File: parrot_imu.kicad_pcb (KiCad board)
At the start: 2 copper layers, 50 x 100 mm, 29 parts, among them J1 Conn_01x02_Male, J2 SI-60062-F, J3 TB005-762-02BE, U1 TR05S3V3, U2 VR10S05, U3 Spark_fun_ICM-20948, U4 Teensy4.1, U5 TJA1441AT/0Z, U6 ESDCAN24-2BLY

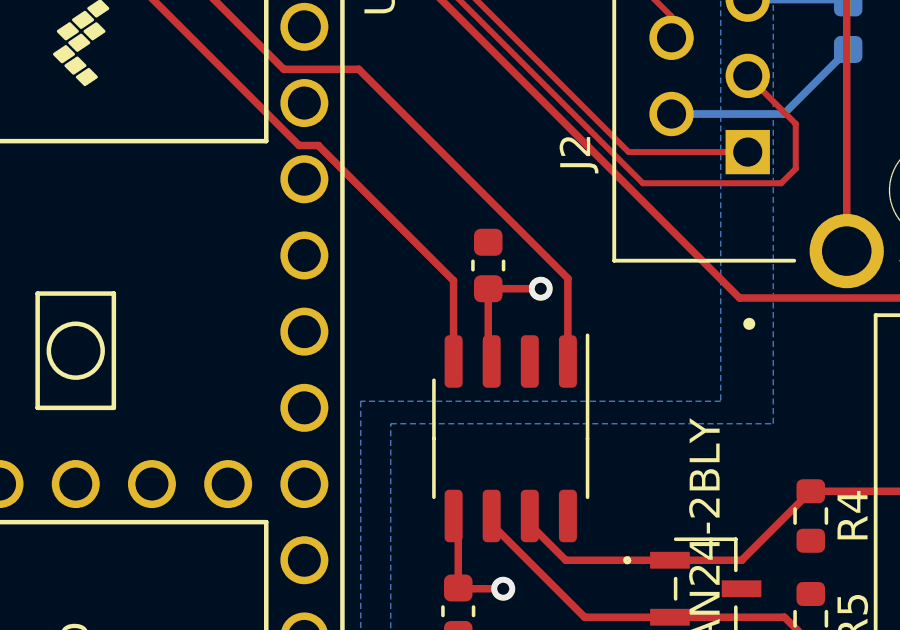
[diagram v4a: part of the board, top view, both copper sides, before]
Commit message: fix unconnected plane error
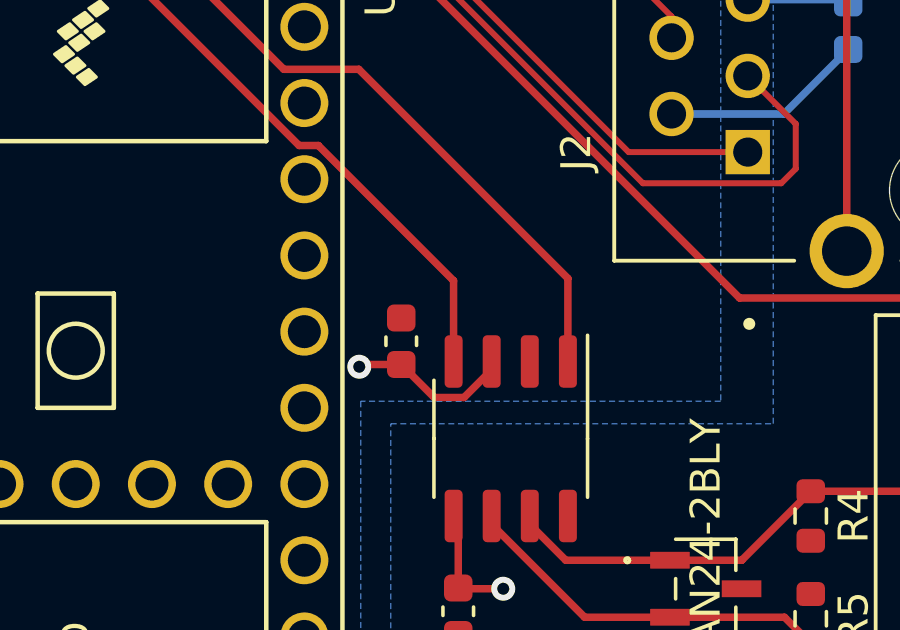
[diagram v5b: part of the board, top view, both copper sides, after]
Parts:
- moved C5 3.85 mm to (70.8, 101.2)
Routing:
- net +5V: track 12.0 -> 13.4 mm
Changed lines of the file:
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@@
   )
   (footprint "Capacitor_SMD:C_0603_1608Metric" (layer "F.Cu")
-    (at 73.75 98.725 90)
+    (at 70.85 101.25 90)
     (descr "Capacitor SMD 0603 (1608 Metric), square (rectangular) end terminal, IPC_7351 nominal, (Body size source: IPC-SM-782 page 76, https://www.pcb-3d.com/wordpress/wp-content/uploads/ipc-sm-782a_amendment_1_and_2.pdf), generated with kicad-footprint-generator")
     (tags "capacitor")
@@
   (segment (start 79.86 86.055) (end 87.191571 86.055) (width 0.25) (layer "B.Cu") (net 2))
   (segment (start 85.64 89.865) (end 85.75 89.975) (width 0.25) (layer "B.Cu") (net 2))
-  (segment (start 73.75 101.81) (end 73.865 101.925) (width 0.25) (layer "F.Cu") (net 3))
   (segment (start 59.5 121.75) (end 61.425 121.75) (width 0.25) (layer "F.Cu") (net 3))
+  (segment (start 70.85 102.025) (end 71.95 103.125) (width 0.25) (layer "F.Cu") (net 3))
   (segment (start 59.776393 130.46) (end 56.316393 127) (width 0.25) (layer "F.Cu") (net 3))
-  (segment (start 75.5 99.5) (end 73.75 99.5) (width 0.25) (layer "F.Cu") (net 3))
+  (segment (start 72.941751 103.125) (end 73.865 102.201751) (width 0.25) (layer "F.Cu") (net 3))
   (segment (start 56.316393 127) (end 55.43238 127) (width 0.25) (layer "F.Cu") (net 3))
-  (segment (start 73.75 99.5) (end 73.75 101.81) (width 0.25) (layer "F.Cu") (net 3))
+  (segment (start 70.85 102.025) (end 69.525 102.025) (width 0.25) (layer "F.Cu") (net 3))
+  (segment (start 69.525 102.025) (end 69.45 102.1) (width 0.25) (layer "F.Cu") (net 3))
   (segment (start 61.425 121.75) (end 61.5 121.675) (width 0.25) (layer "F.Cu") (net 3))
+  (segment (start 73.865 102.201751) (end 73.865 101.925) (width 0.25) (layer "F.Cu") (net 3))
+  (segment (start 71.95 103.125) (end 72.941751 103.125) (width 0.25) (layer "F.Cu") (net 3))
   (via (at 59.5 121.75) (size 0.8) (drill 0.4) (layers "F.Cu" "B.Cu") (free) (net 3))
-  (via (at 75.5 99.5) (size 0.8) (drill 0.4) (layers "F.Cu" "B.Cu") (free) (net 3))
+  (via (at 69.45 102.1) (size 0.8) (drill 0.4) (layers "F.Cu" "B.Cu") (free) (net 3))
   (segment (start 91.915 117.835) (end 92 117.75) (width 0.25) (layer "F.Cu") (net 4))
   (segment (start 72.775 109.5) (end 72.75 109.475) (width 0.25) (layer "F.Cu") (net 4))

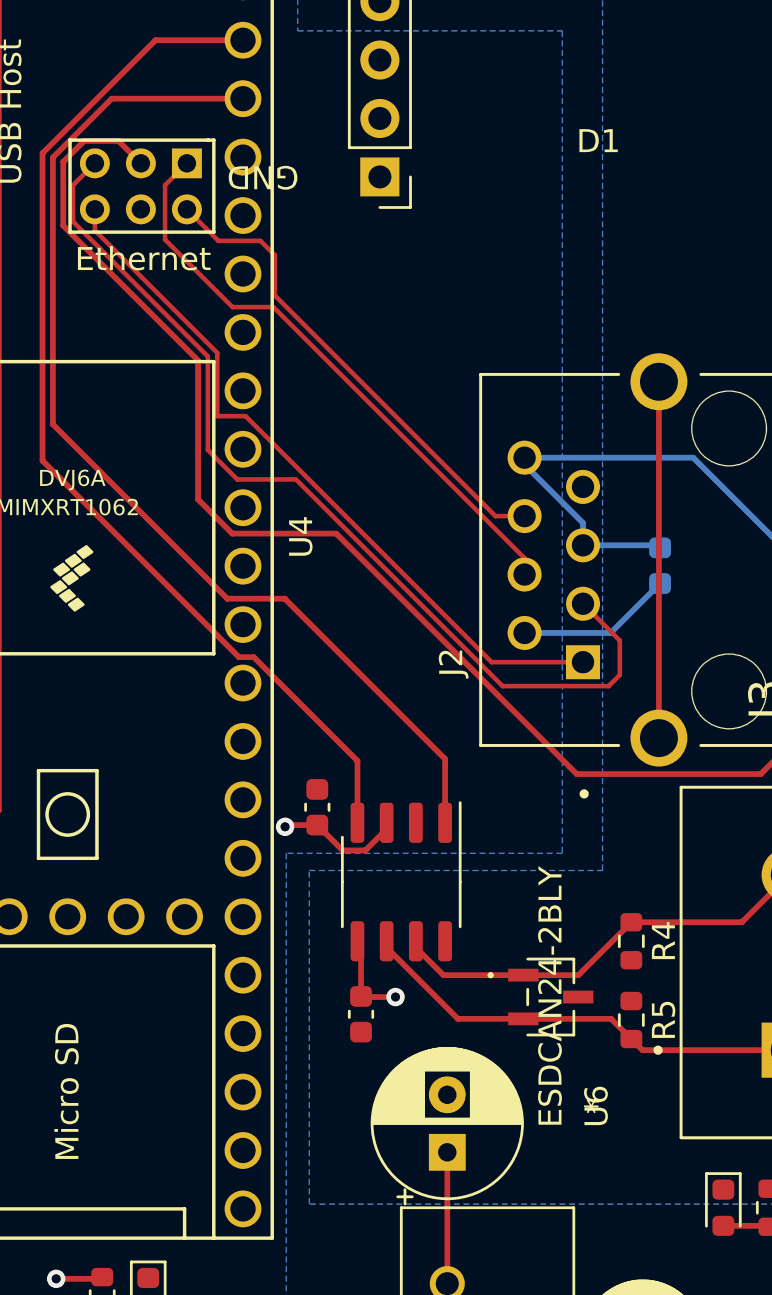
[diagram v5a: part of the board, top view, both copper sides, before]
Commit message: fix errors with unconnected components
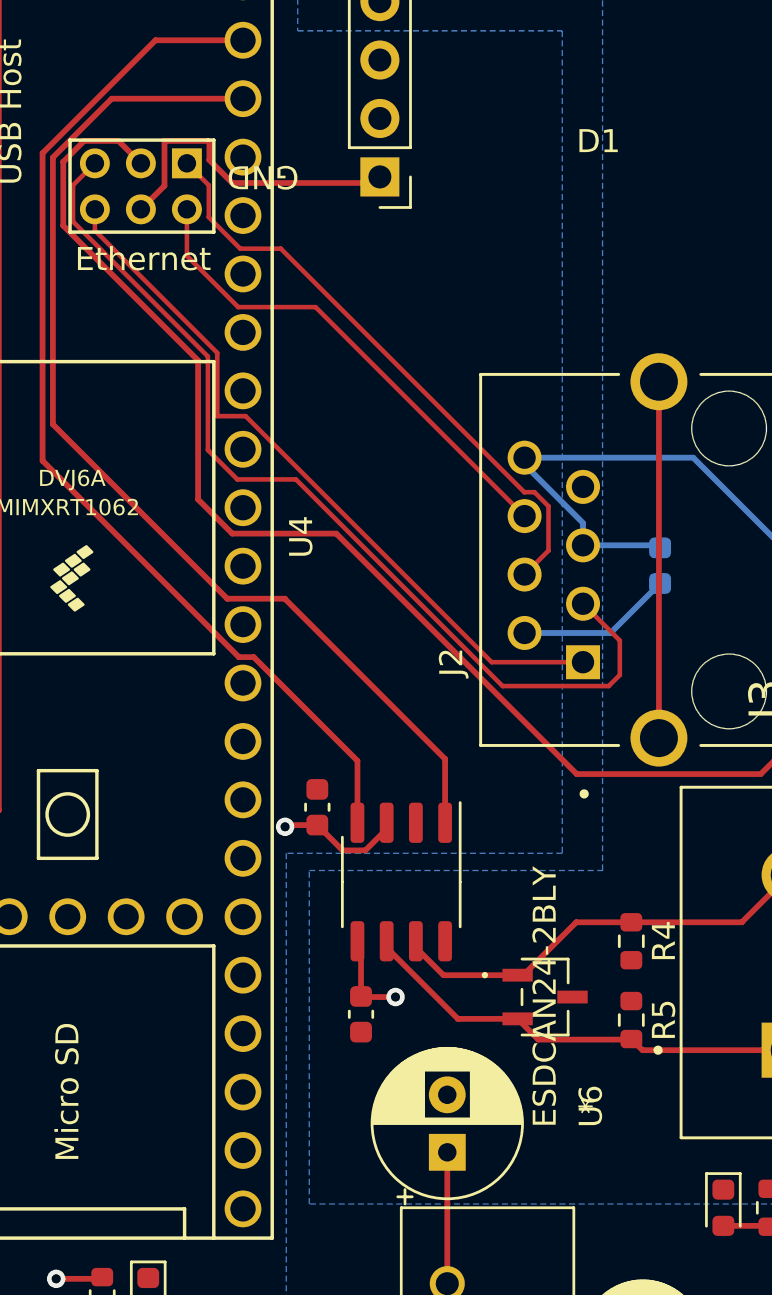
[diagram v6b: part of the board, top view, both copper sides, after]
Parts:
- moved U6 0.25 mm to (80.8, 109.5)
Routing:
- net GND: track 31.7 -> 45.8 mm
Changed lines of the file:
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@@
   )
   (footprint "parrot_imu:ESDCAN24-2BLY" (layer "F.Cu")
-    (at 81 109.5 -90)
+    (at 80.75 109.5 -90)
     (property "Sheetfile" "parrot_imu.kicad_sch")
     (property "Sheetname" "")
@@
   (segment (start 84 130) (end 76.5 130) (width 0.25) (layer "F.Cu") (net 1))
   (segment (start 59.816393 135.5) (end 59.776393 135.54) (width 0.25) (layer "F.Cu") (net 1))
+  (segment (start 64.2066 72.285) (end 64.2066 74.235) (width 0.25) (layer "F.Cu") (net 2))
+  (segment (start 66.1566 73.117591) (end 66.1566 72.285) (width 0.25) (layer "F.Cu") (net 2))
   (segment (start 93 125.625) (end 93 124.4125) (width 0.25) (layer "F.Cu") (net 2))
+  (segment (start 66.1566 72.285) (end 64.2066 72.285) (width 0.25) (layer "F.Cu") (net 2))
+  (segment (start 64.2066 74.235) (end 63.1816 75.26) (width 0.25) (layer "F.Cu") (net 2))
+  (segment (start 73.57 73.85) (end 73.305 74.115) (width 0.25) (layer "F.Cu") (net 2))
+  (segment (start 73.305 74.115) (end 67.154009 74.115) (width 0.25) (layer "F.Cu") (net 2))
   (segment (start 88 130) (end 92 130) (width 0.25) (layer "F.Cu") (net 2))
+  (segment (start 67.154009 74.115) (end 66.1566 73.117591) (width 0.25) (layer "F.Cu") (net 2))
   (via (at 92 130) (size 0.8) (drill 0.4) (layers "F.Cu" "B.Cu") (free) (net 2))
   (via (at 93 124.4125) (size 0.8) (drill 0.4) (layers "F.Cu" "B.Cu") (free) (net 2))
@@
   (segment (start 60.2316 74.21) (end 60.2316 75.794924) (width 0.2) (layer "F.Cu") (net 10))
   (segment (start 60.2316 75.794924) (end 66.093338 81.656662) (width 0.2) (layer "F.Cu") (net 10))
-  (segment (start 64.2316 74.21) (end 64.2316 76.577235) (width 0.2) (layer "F.Cu") (net 11))
-  (segment (start 65.1816 73.26) (end 64.2316 74.21) (width 0.2) (layer "F.Cu") (net 11))
-  (segment (start 79.86 90.425686) (end 79.86 91.135) (width 0.2) (layer "F.Cu") (net 11))
-  (segment (start 67.164365 79.51) (end 68.944314 79.51) (width 0.2) (layer "F.Cu") (net 11))
-  (segment (start 64.2316 76.577235) (end 67.164365 79.51) (width 0.2) (layer "F.Cu") (net 11))
-  (segment (start 68.944314 79.51) (end 79.86 90.425686) (width 0.2) (layer "F.Cu") (net 11))
-  (segment (start 78.595 88.595) (end 69 79) (width 0.2) (layer "F.Cu") (net 12))
-  (segment (start 79.86 88.595) (end 78.595 88.595) (width 0.2) (layer "F.Cu") (net 12))
-  (segment (start 69 77.25) (end 68.38 76.63) (width 0.2) (layer "F.Cu") (net 12))
-  (segment (start 69 79) (end 69 77.25) (width 0.2) (layer "F.Cu") (net 12))
-  (segment (start 66.5516 76.63) (end 65.1816 75.26) (width 0.2) (layer "F.Cu") (net 12))
-  (segment (start 68.38 76.63) (end 66.5516 76.63) (width 0.2) (layer "F.Cu") (net 12))
+  (segment (start 80.899 88.164632) (end 80.899 90.096) (width 0.2) (layer "F.Cu") (net 11))
+  (segment (start 80.290368 87.556) (end 80.899 88.164632) (width 0.2) (layer "F.Cu") (net 11))
+  (segment (start 79.85 87.556) (end 80.290368 87.556) (width 0.2) (layer "F.Cu") (net 11))
+  (segment (start 66.1316 74.21) (end 66.1316 75.6016) (width 0.2) (layer "F.Cu") (net 11))
+  (segment (start 69.264 76.97) (end 79.85 87.556) (width 0.2) (layer "F.Cu") (net 11))
+  (segment (start 66.1316 75.6016) (end 67.5 76.97) (width 0.2) (layer "F.Cu") (net 11))
+  (segment (start 67.5 76.97) (end 69.264 76.97) (width 0.2) (layer "F.Cu") (net 11))
+  (segment (start 65.1816 73.26) (end 66.1316 74.21) (width 0.2) (layer "F.Cu") (net 11))
+  (segment (start 80.899 90.096) (end 79.86 91.135) (width 0.2) (layer "F.Cu") (net 11))
+  (segment (start 65.1816 75.26) (end 65.1816 77.2816) (width 0.2) (layer "F.Cu") (net 12))
+  (segment (start 70.775 79.51) (end 79.86 88.595) (width 0.2) (layer "F.Cu") (net 12))
+  (segment (start 67.41 79.51) (end 70.775 79.51) (width 0.2) (layer "F.Cu") (net 12))
+  (segment (start 65.1816 77.2816) (end 67.41 79.51) (width 0.2) (layer "F.Cu") (net 12))
+  (segment (start 84.5 111.325) (end 84.985 111.81) (width 0.25) (layer "F.Cu") (net 13))
+  (segment (start 84.475 111.35) (end 84.5 111.325) (width 0.25) (layer "F.Cu") (net 13))
+  (segment (start 73.865 107.075) (end 73.865 107.351751) (width 0.25) (layer "F.Cu") (net 13))
+  (segment (start 80.45624 111.35) (end 84.475 111.35) (width 0.25) (layer "F.Cu") (net 13))
+  (segment (start 79.5562 110.44996) (end 80.45624 111.35) (width 0.25) (layer "F.Cu") (net 13))
   (segment (start 73.865 107.351751) (end 76.963209 110.44996) (width 0.25) (layer "F.Cu") (net 13))
-  (segment (start 83.62496 110.44996) (end 84.5 111.325) (width 0.25) (layer "F.Cu") (net 13))
-  (segment (start 73.865 107.075) (end 73.865 107.351751) (width 0.25) (layer "F.Cu") (net 13))
-  (segment (start 84.5 111.325) (end 84.985 111.81) (width 0.25) (layer "F.Cu") (net 13))
-  (segment (start 76.963209 110.44996) (end 79.8062 110.44996) (width 0.25) (layer "F.Cu") (net 13))
-  (segment (start 79.8062 110.44996) (end 83.62496 110.44996) (width 0.25) (layer "F.Cu") (net 13))
+  (segment (start 76.963209 110.44996) (end 79.5562 110.44996) (width 0.25) (layer "F.Cu") (net 13))
   (segment (start 84.985 111.81) (end 91.3625 111.81) (width 0.25) (layer "F.Cu") (net 13))
+  (segment (start 89.3025 106.25) (end 91.3625 104.19) (width 0.25) (layer "F.Cu") (net 14))
+  (segment (start 82.10624 106.25) (end 84.5 106.25) (width 0.25) (layer "F.Cu") (net 14))
   (segment (start 75.135 107.075) (end 75.135 107.351751) (width 0.25) (layer "F.Cu") (net 14))
-  (segment (start 82.19996 108.55004) (end 84.5 106.25) (width 0.25) (layer "F.Cu") (net 14))
-  (segment (start 76.333289 108.55004) (end 79.8062 108.55004) (width 0.25) (layer "F.Cu") (net 14))
-  (segment (start 89.3025 106.25) (end 91.3625 104.19) (width 0.25) (layer "F.Cu") (net 14))
   (segment (start 75.135 107.351751) (end 76.333289 108.55004) (width 0.25) (layer "F.Cu") (net 14))
   (segment (start 84.5 106.25) (end 89.3025 106.25) (width 0.25) (layer "F.Cu") (net 14))
-  (segment (start 79.8062 108.55004) (end 82.19996 108.55004) (width 0.25) (layer "F.Cu") (net 14))
+  (segment (start 79.8062 108.55004) (end 82.10624 106.25) (width 0.25) (layer "F.Cu") (net 14))
+  (segment (start 76.333289 108.55004) (end 79.8062 108.55004) (width 0.25) (layer "F.Cu") (net 14))
   (segment (start 99.25 52.75) (end 99.25 61.5) (width 0.25) (layer "F.Cu") (net 19))
   (segment (start 52.38 62.83) (end 64.71 50.5) (width 0.25) (layer "F.Cu") (net 19))

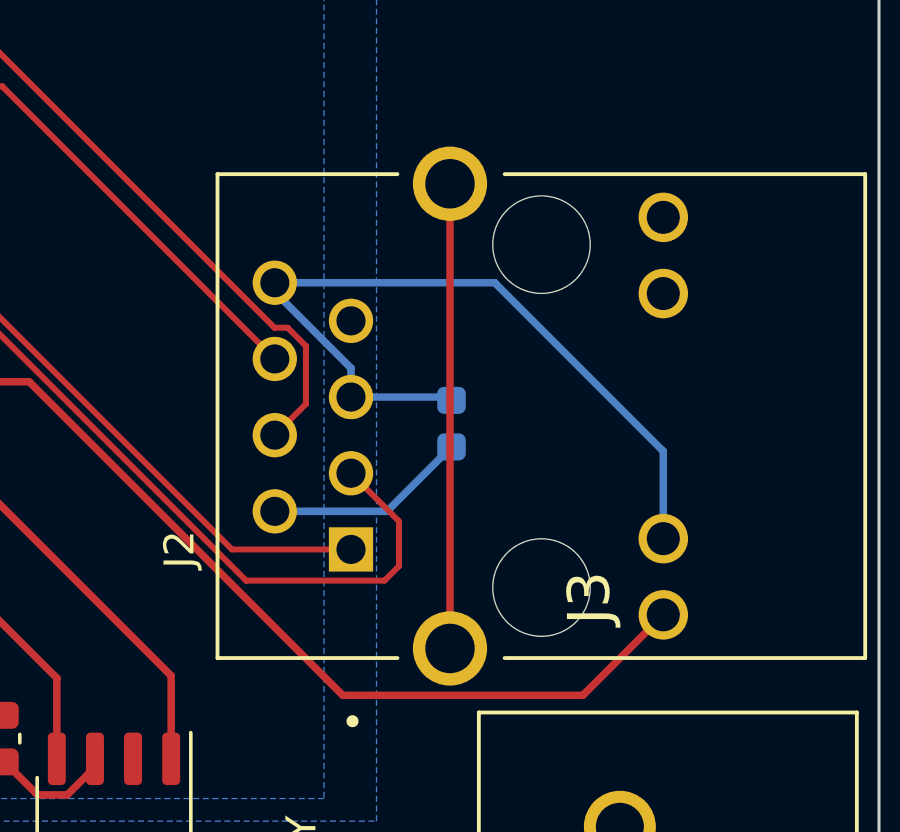
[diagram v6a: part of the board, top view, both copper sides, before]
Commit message: removed trace between shield on ethernet
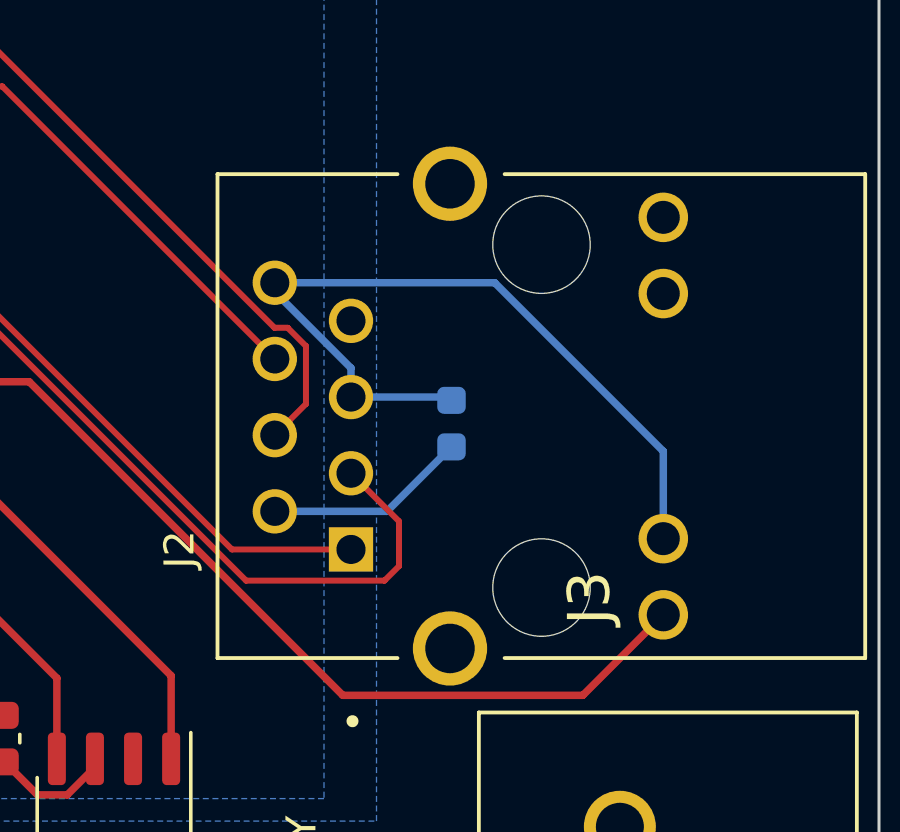
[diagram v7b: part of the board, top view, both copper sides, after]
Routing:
- net unconnected-(J2-PadS1): track 15.5 -> 0.00 mm
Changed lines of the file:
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@@
   (segment (start 82.126409 99.8075) (end 90.1275 99.8075) (width 0.25) (layer "F.Cu") (net 69))
   (segment (start 63.1816 73.26) (end 62.2066 72.285) (width 0.25) (layer "F.Cu") (net 69))
-  (segment (start 85.7 98.245) (end 85.7 82.755) (width 0.25) (layer "F.Cu") (net 79))
   (zone (net 2) (net_name "GND") (layer "F.Cu") (hatch edge 0.508)
     (connect_pads (clearance 0.508))

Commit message: dump of progress
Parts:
- C6: moved to F.Cu
- J1: footprint Connector_AMASS:AMASS_XT30PW-F_1x02_P2.50mm_Horizontal -> Connector_AMASS:AMASS_XT30PW-M_1x02_P2.50mm_Horizontal
- moved D2 30.8 mm to (68.5, 145.0)
- moved R1 30.8 mm to (66.5, 145.1)
- moved R2 29.3 mm to (62.1, 126.0), turned to 0 degrees
- moved D3 28.0 mm to (62.1, 128.0), turned to 0 degrees
- moved U1 26.2 mm to (52.4, 134.7)
- moved C1 26.2 mm to (61.6, 137.2)
- moved C4 23.3 mm to (55.4, 126.0)
- moved U3 20.0 mm to (85.6, 84.8), turned to -90 degrees
- moved C5 18.6 mm to (74.0, 119.5), turned to 0 degrees
- moved D1 18.5 mm to (74.1, 144.2), turned to 180 degrees
- moved R3 15.6 mm to (76.7, 126.0), turned to 0 degrees
- moved D4 14.4 mm to (76.8, 128.1), turned to 0 degrees
- moved C3 14.3 mm to (69.7, 126.0), turned to 90 degrees
- moved C6 12.3 mm to (75.6, 97.8)
- moved U5 11.1 mm to (73.9, 115.6), turned to 0 degrees
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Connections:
- U4 pad 22: unconnected-(U4-Pad22) -> /Can_rx
- U4 pad 23: unconnected-(U4-Pad23) -> /Can_tx
- U4 pad 44: /Can_tx -> unconnected-(U4-Pad44)
- U4 pad 45: /Can_rx -> unconnected-(U4-Pad45)
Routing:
- net +5V: track 13.4 -> 162.9 mm, vias 2 -> 1
- net /Eth_led: track 54.5 -> 0.00 mm
- net /SCK: track 118.3 -> 67.2 mm
- net /MOSI: track 110.6 -> 65.5 mm
- net /Eth_tx-: track 41.4 -> 0.00 mm
- net /MISO: track 68.6 -> 30.6 mm
- net /CS: track 64.6 -> 27.1 mm
- net /Eth_tx+: track 31.5 -> 0.00 mm
- net /Can_tx: track 46.8 -> 20.6 mm
- net /Eth_rx+: track 26.1 -> 0.00 mm
- net /Can_rx: track 45.9 -> 24.0 mm
- net /Eth_rx-: track 21.4 -> 0.00 mm
- net Net-(C1-Pad1): track 51.2 -> 62.2 mm
- net +3.3V: track 11.2 -> 7.34 mm, vias 2 -> 0
- net Net-(J3-Pad1): track 19.6 -> 15.8 mm
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- added copper zone on F.Cu, net +3.3V
- added copper zone on B.Cu, net GND
- removed copper zone on B.Cu, net +3.3V
- removed copper zone on B.Cu, net +5V
- removed copper zone on F.Cu, net GND
